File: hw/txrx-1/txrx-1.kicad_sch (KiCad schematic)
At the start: 8 parts, among them J1 Conn_01x04, J2 Conn_01x03, J3 Conn_01x02, J4 Conn_01x08

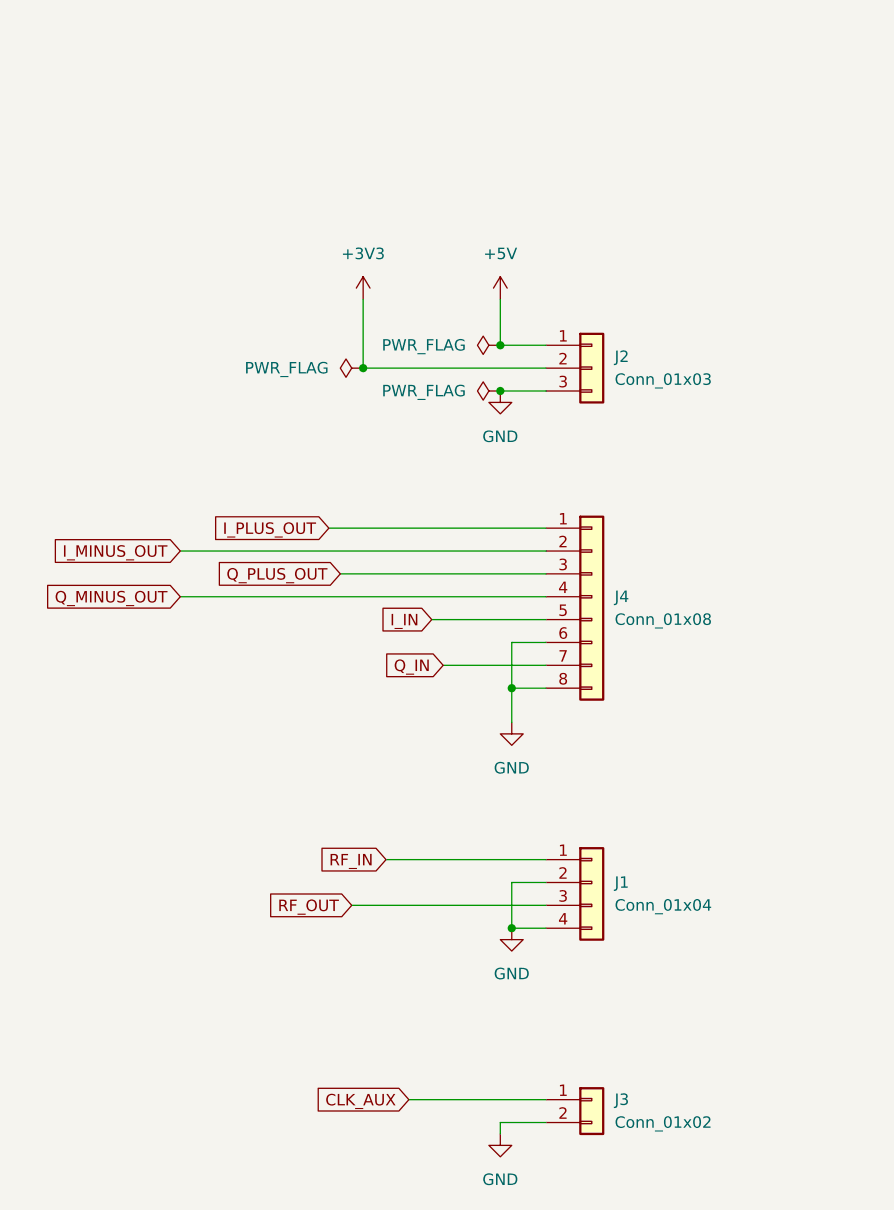
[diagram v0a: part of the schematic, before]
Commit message: Initial PCB layout for TXRX board
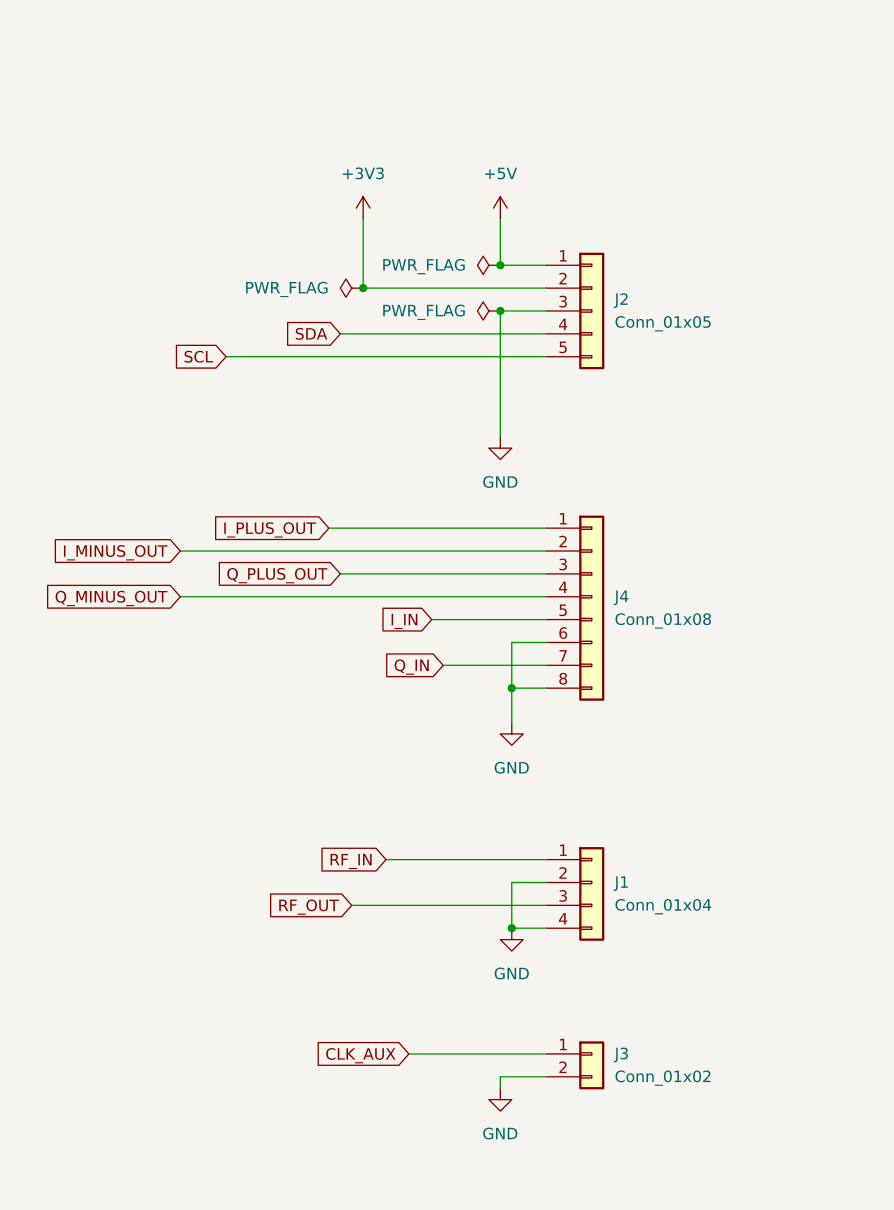
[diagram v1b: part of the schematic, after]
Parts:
- removed J2: Conn_01x03, symbol Connector_Generic:Conn_01x03
- added J2: Conn_01x05, Connector_PinHeader_2.54mm:PinHeader_1x05_P2.54mm_Vertical, symbol Connector_Generic:Conn_01x05
- J1: footprint (none) -> Connector_PinHeader_2.54mm:PinHeader_1x04_P2.54mm_Vertical
- J3: footprint (none) -> Connector_PinHeader_2.54mm:PinHeader_1x02_P2.54mm_Vertical
- J4: footprint (none) -> Connector_PinHeader_2.54mm:PinHeader_1x08_P2.54mm_Vertical
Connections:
- net +3V3: now also J2.2 (Pin_2)
- net +5V: now also J2.1 (Pin_1)
- net GND: now also J2.3 (Pin_3)
- new net SCL: J2.5 (Pin_5)
- new net SDA: J2.4 (Pin_4)
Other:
- company: (none) -> Bruce MacKinnon KC1FSZ
- title: (none) -> Quadrature TX/RX Board
- moved on the sheet: J3
